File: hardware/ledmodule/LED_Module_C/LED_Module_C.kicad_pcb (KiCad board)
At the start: 4 copper layers, 70 x 79.1 mm, 100 parts, among them J26 Conn_01x04_Pin, U1 TMP1075DSG

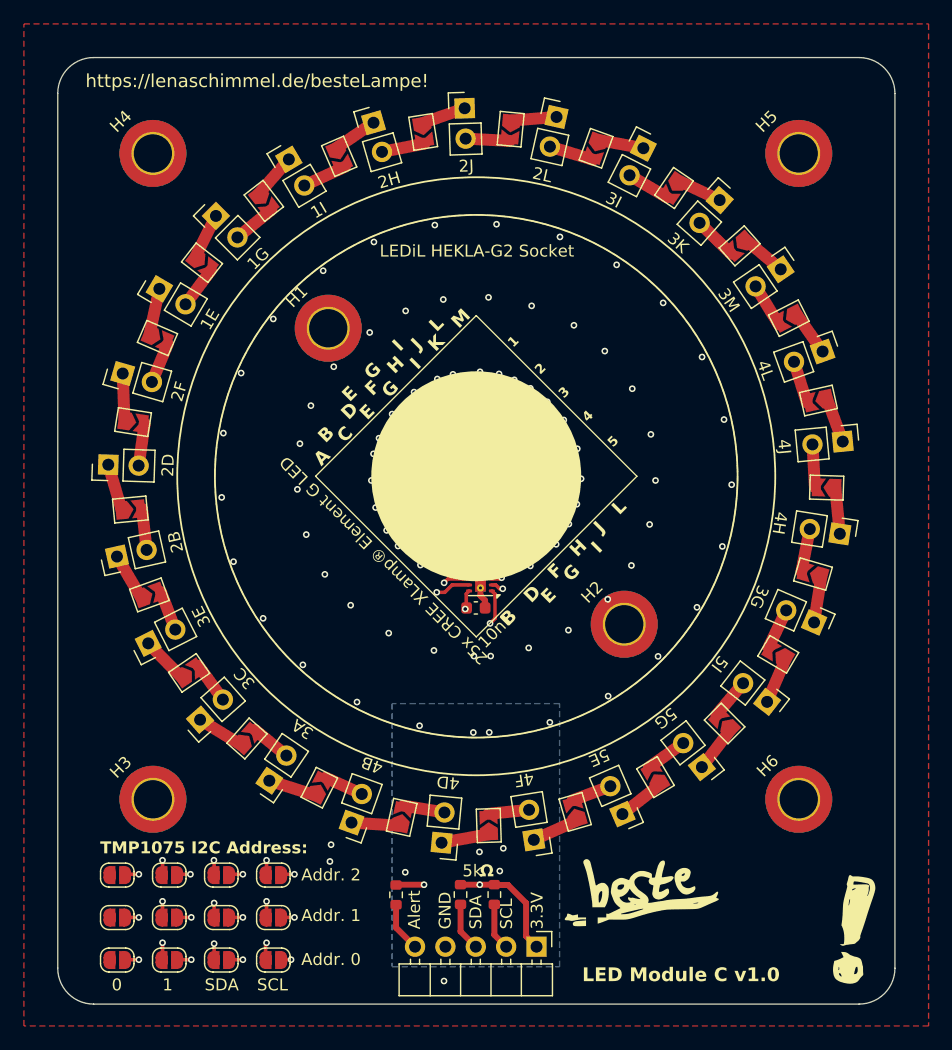
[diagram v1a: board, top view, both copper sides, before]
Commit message: Several changes to LED modules A2 and C, two items added to the library. Readme updated.
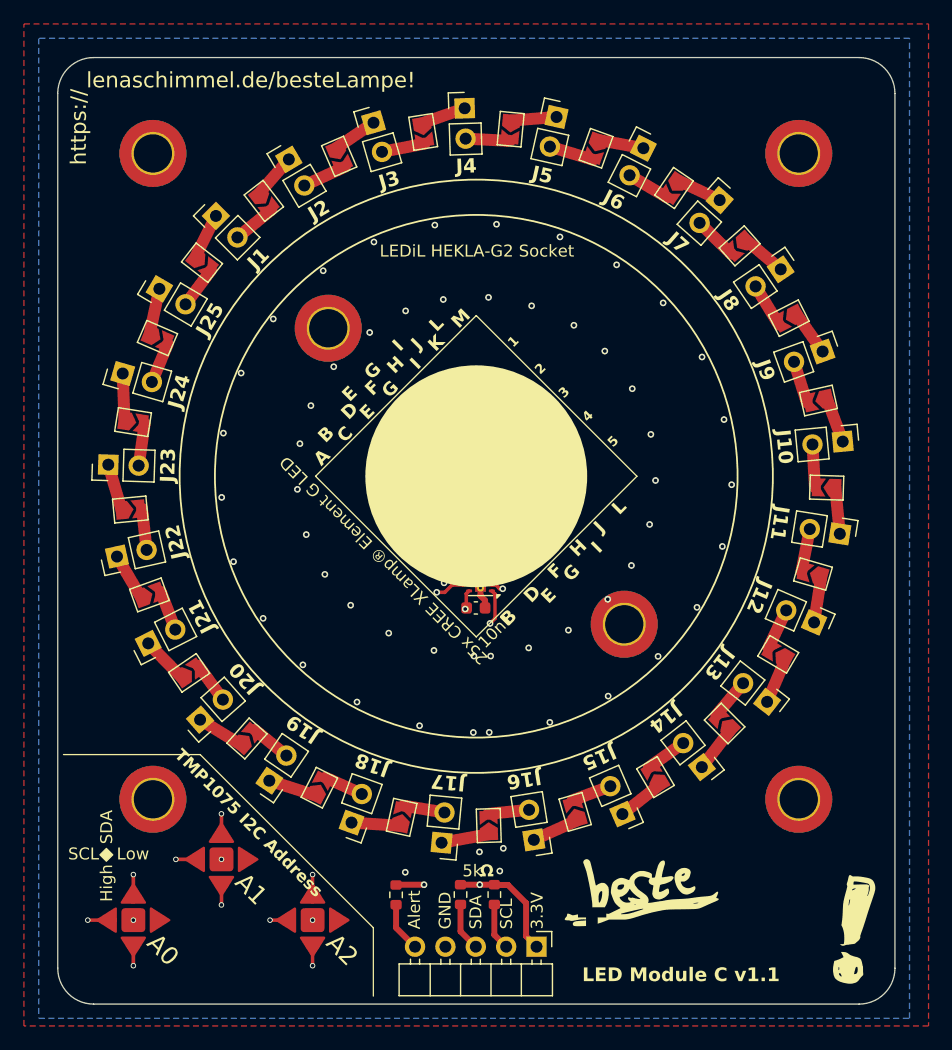
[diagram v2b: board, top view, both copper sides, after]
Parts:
- removed AC0, AC1, AC2, AD0, AD1, AD2, AH0, AH1, AH2, AL0, AL1, AL2: ~, Jumper:SolderJumper-2_P1.3mm_Open_RoundedPad1.0x1.5mm
- added J27: Conn_01x05, Jumper:Quadforce, F.Cu at (71.4, 137.2)
- added J28: Conn_01x05, Jumper:Quadforce, F.Cu at (78.7, 132.1)
- added J29: Conn_01x05, Jumper:Quadforce, F.Cu at (86.4, 137.2)
- renumbered 1G to J1, 4J to J10, 4H to J11, 3G to J12, 5I to J13, 5G to J14, 5E to J15, 4F to J16, 4D to J17, 4B to J18, 3A to J19, 1I to J2, 3C to J20, 3E to J21, 2B to J22, 2D to J23, 2F to J24, 1E to J25, 2H to J3, 2J to J4, 2L to J5, 3I to J6, 3K to J7, 3M to J8, 4L to J9
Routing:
- net /SCL: track 67.8 -> 90.0 mm
- net /A2: track 53.6 -> 36.4 mm, vias 5 -> 2
- net /A1: track 55.3 -> 41.0 mm, vias 6 -> 2
- net /A0: track 58.4 -> 49.1 mm, vias 6 -> 2
- net /SDA: track 69.5 -> 75.8 mm
- net +3.3V: track 86.5 -> 85.4 mm
- net GND: vias 138 -> 137
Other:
- board text added: "A0"
- board text added: "A1"
- board text added: "A2"
- board text added: "High"
- board text added: "LED Module C v1.1"
- board text added: "Low"
- board text added: "TMP1075 I2C Address"
- board text added: "https://"
- board text added: "lenaschimmel.de/besteLampe!"
- board text removed: "0"
- board text removed: "Addr. 0"
- board text removed: "Addr. 1"
- board text removed: "Addr. 2"
- board text removed: "LED Module C v1.0"
- board text removed: "TMP1075 I2C Address:"
- board text removed: "https://lenaschimmel.de/besteLampe!"
